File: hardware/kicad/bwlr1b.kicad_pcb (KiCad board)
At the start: 2 copper layers, 38.6 x 72.1 mm, 41 parts, among them J3 915MHz SMA, Q1 AO3407, SW3 RESET, SW4 BOOT, U1 BME680, U2 RAK3172

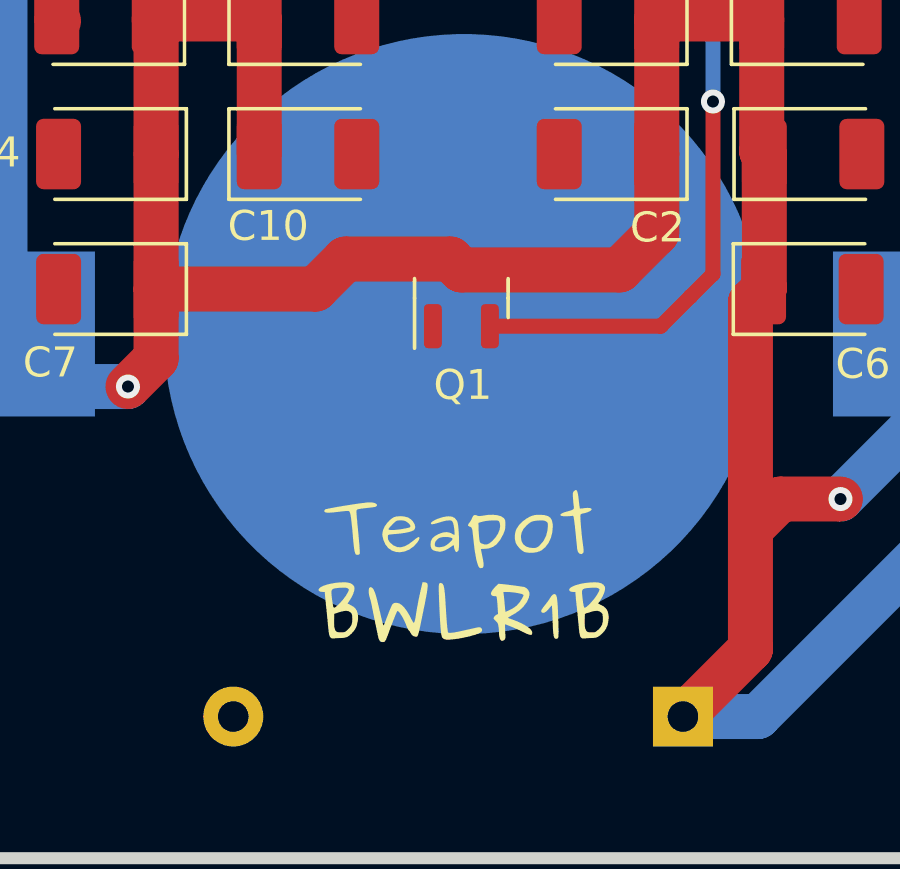
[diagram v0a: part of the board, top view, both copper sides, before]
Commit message: update logo
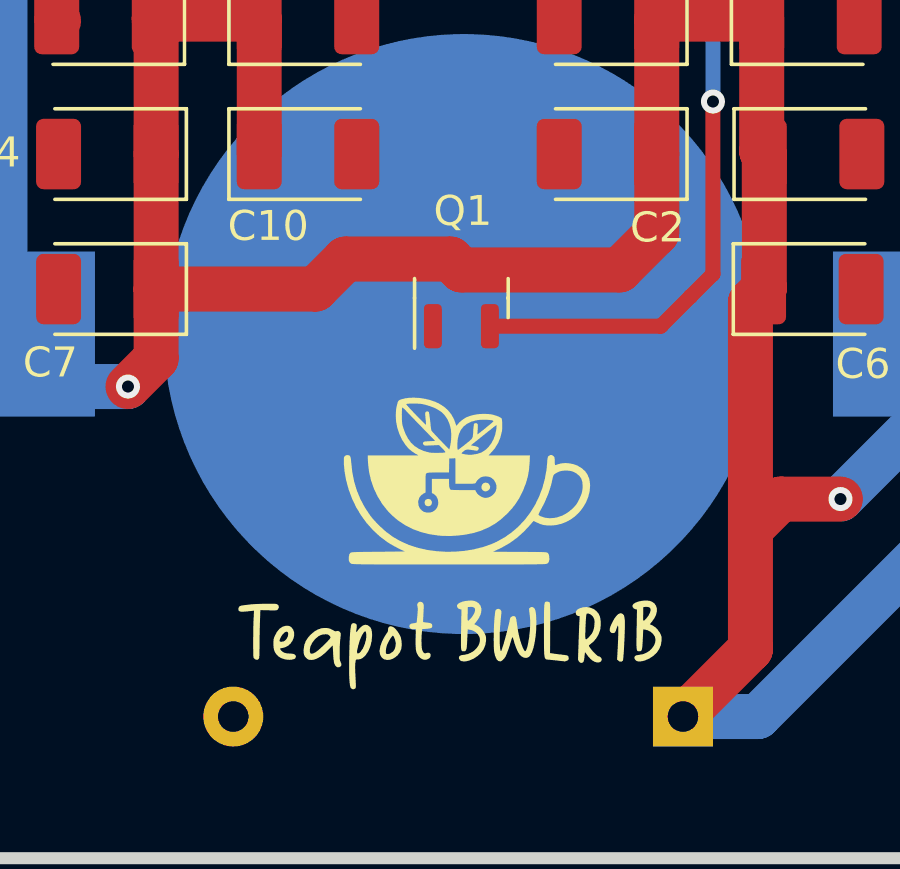
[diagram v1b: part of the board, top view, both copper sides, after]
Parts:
- removed REF**: TextLogo_Teapot, Teapot:TextLogo_Teapot
- added G***: LOGO, Teapot:TeapotLogo, F.Cu at (152.8, 96.3)
- added G***: LOGO, Teapot:TextLogo_Teapot, F.Cu at (149.1, 101.9)
- moved G*** 3.25 mm to (156.4, 101.4)
